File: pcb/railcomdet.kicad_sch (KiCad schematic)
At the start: 43 parts, among them J1 MVE252-5-V, J10 MVE252-5-V, J2 MVE252-5-V, J3 MVE252-5-V, J7 MVE252-5-V, J8 MVE252-5-V, J9 MVE252-5-V, U1 VO0631T, U2 VO0631T, U3 VO0631T

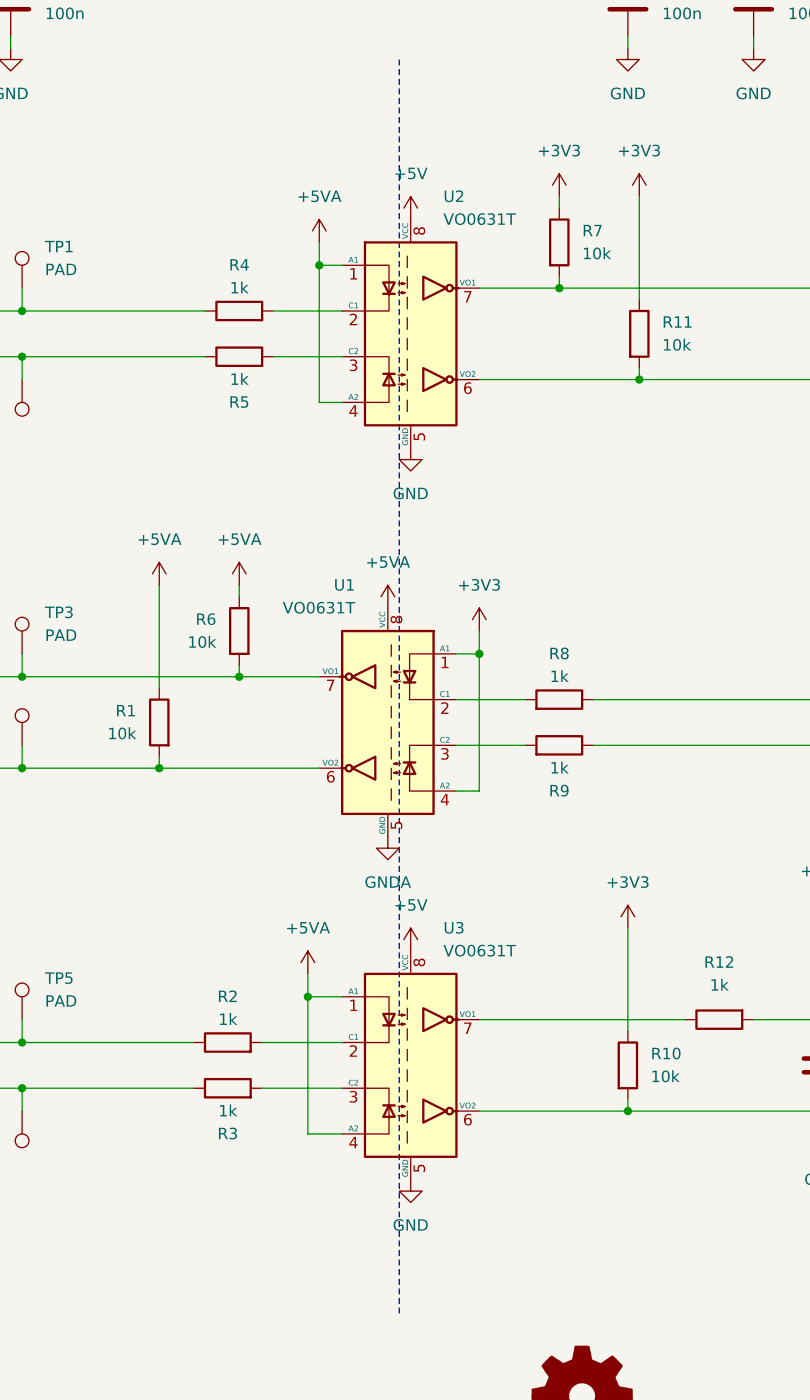
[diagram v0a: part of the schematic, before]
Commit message: Added Sch.diodes, text editing..
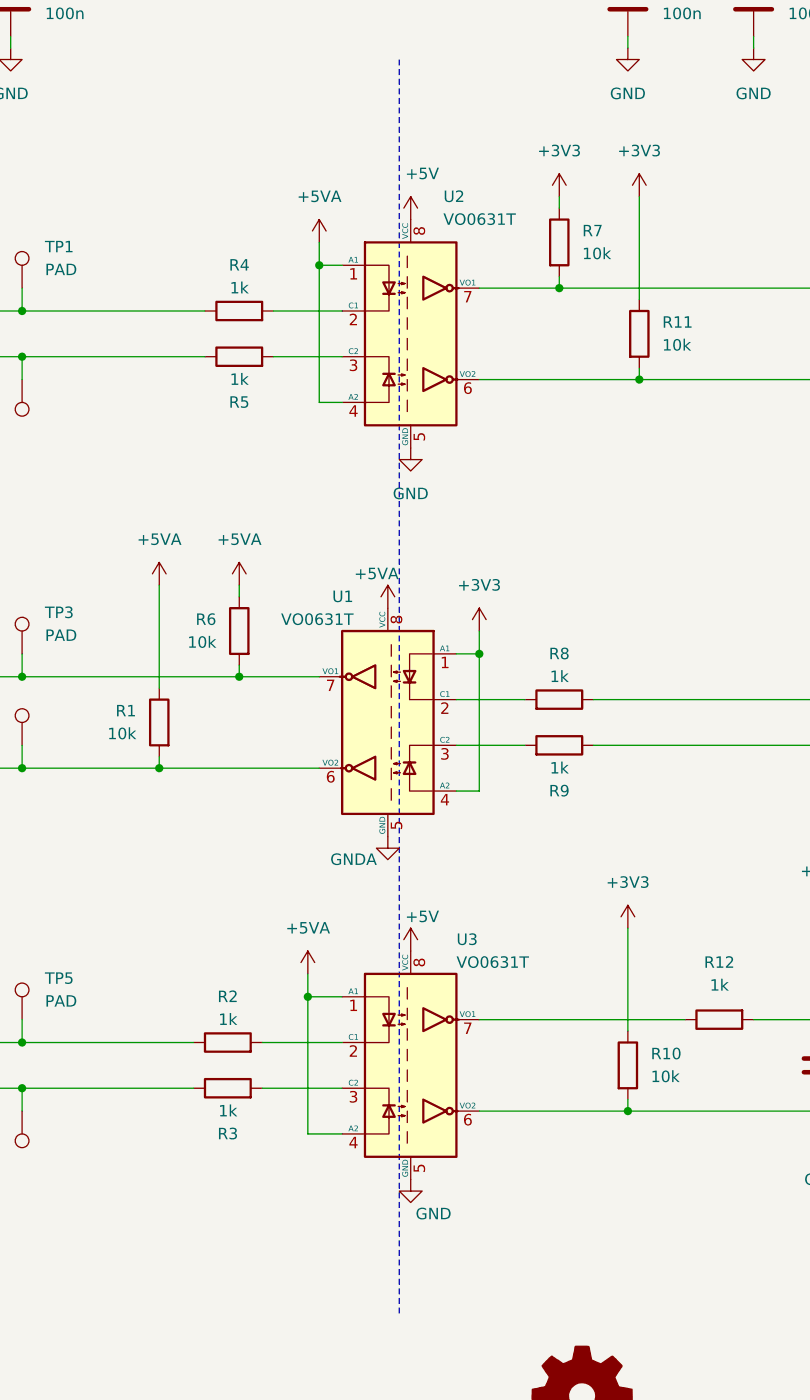
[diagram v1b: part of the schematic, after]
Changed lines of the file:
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@@
   )
   (symbol (lib_id "Isolator:VO0631T") (at 143.51 106.68 0) (mirror y) (unit 1)
-    (in_bom yes) (on_board yes) (dnp no) (fields_autoplaced)
-    (property "Reference" "U1" (at 139.8839 91.44 0)
-      (effects (font (size 1.27 1.27)) (justify left))
-    )
-    (property "Value" "VO0631T" (at 139.8839 93.98 0)
+    (in_bom yes) (on_board yes) (dnp no)
+    (property "Reference" "U1" (at 139.7 92.71 0)
+      (effects (font (size 1.27 1.27)) (justify left))
+    )
+    (property "Value" "VO0631T" (at 139.7 95.25 0)
       (effects (font (size 1.27 1.27)) (justify left))
     )
@@
   )
   (symbol (lib_id "power:GND") (at 146.05 157.48 0) (unit 1)
-    (in_bom yes) (on_board yes) (dnp no) (fields_autoplaced)
+    (in_bom yes) (on_board yes) (dnp no)
     (property "Reference" "#PWR012" (at 146.05 163.83 0)
       (effects (font (size 1.27 1.27)) hide)
     )
-    (property "Value" "GND" (at 146.05 162.56 0)
+    (property "Value" "GND" (at 148.59 161.29 0)
       (effects (font (size 1.27 1.27)))
     )
@@
   )
   (symbol (lib_id "Isolator:VO0631T") (at 146.05 144.78 0) (unit 1)
-    (in_bom yes) (on_board yes) (dnp no) (fields_autoplaced)
-    (property "Reference" "U3" (at 149.6761 129.54 0)
-      (effects (font (size 1.27 1.27)) (justify left))
-    )
-    (property "Value" "VO0631T" (at 149.6761 132.08 0)
+    (in_bom yes) (on_board yes) (dnp no)
+    (property "Reference" "U3" (at 151.13 130.81 0)
+      (effects (font (size 1.27 1.27)) (justify left))
+    )
+    (property "Value" "VO0631T" (at 151.13 133.35 0)
       (effects (font (size 1.27 1.27)) (justify left))
     )
@@
   )
   (symbol (lib_id "power:+5VA") (at 143.51 93.98 0) (unit 1)
-    (in_bom yes) (on_board yes) (dnp no) (fields_autoplaced)
+    (in_bom yes) (on_board yes) (dnp no)
     (property "Reference" "#PWR07" (at 143.51 97.79 0)
       (effects (font (size 1.27 1.27)) hide)
     )
-    (property "Value" "+5VA" (at 143.51 88.9 0)
+    (property "Value" "+5VA" (at 142.24 90.17 0)
       (effects (font (size 1.27 1.27)))
     )
@@
   )
   (symbol (lib_id "power:+5V") (at 146.05 50.8 0) (unit 1)
-    (in_bom yes) (on_board yes) (dnp no) (fields_autoplaced)
+    (in_bom yes) (on_board yes) (dnp no)
     (property "Reference" "#PWR09" (at 146.05 54.61 0)
       (effects (font (size 1.27 1.27)) hide)
     )
-    (property "Value" "+5V" (at 146.05 45.72 0)
+    (property "Value" "+5V" (at 147.32 45.72 0)
       (effects (font (size 1.27 1.27)))
     )
@@
       (effects (font (size 1.27 1.27)) hide)
     )
-    (property "Value" "GNDA" (at 143.51 124.46 0)
+    (property "Value" "GNDA" (at 139.7 121.92 0)
       (effects (font (size 1.27 1.27)))
     )
@@
   )
   (symbol (lib_id "power:+5V") (at 146.05 132.08 0) (unit 1)
-    (in_bom yes) (on_board yes) (dnp no) (fields_autoplaced)
+    (in_bom yes) (on_board yes) (dnp no)
     (property "Reference" "#PWR011" (at 146.05 135.89 0)
       (effects (font (size 1.27 1.27)) hide)
     )
-    (property "Value" "+5V" (at 146.05 127 0)
-      (effects (font (size 1.27 1.27)))
-    )
+    (property "Value" "+5V" (at 147.32 128.27 0)
+      (effects (font (size 1.27 1.27)))
+    )

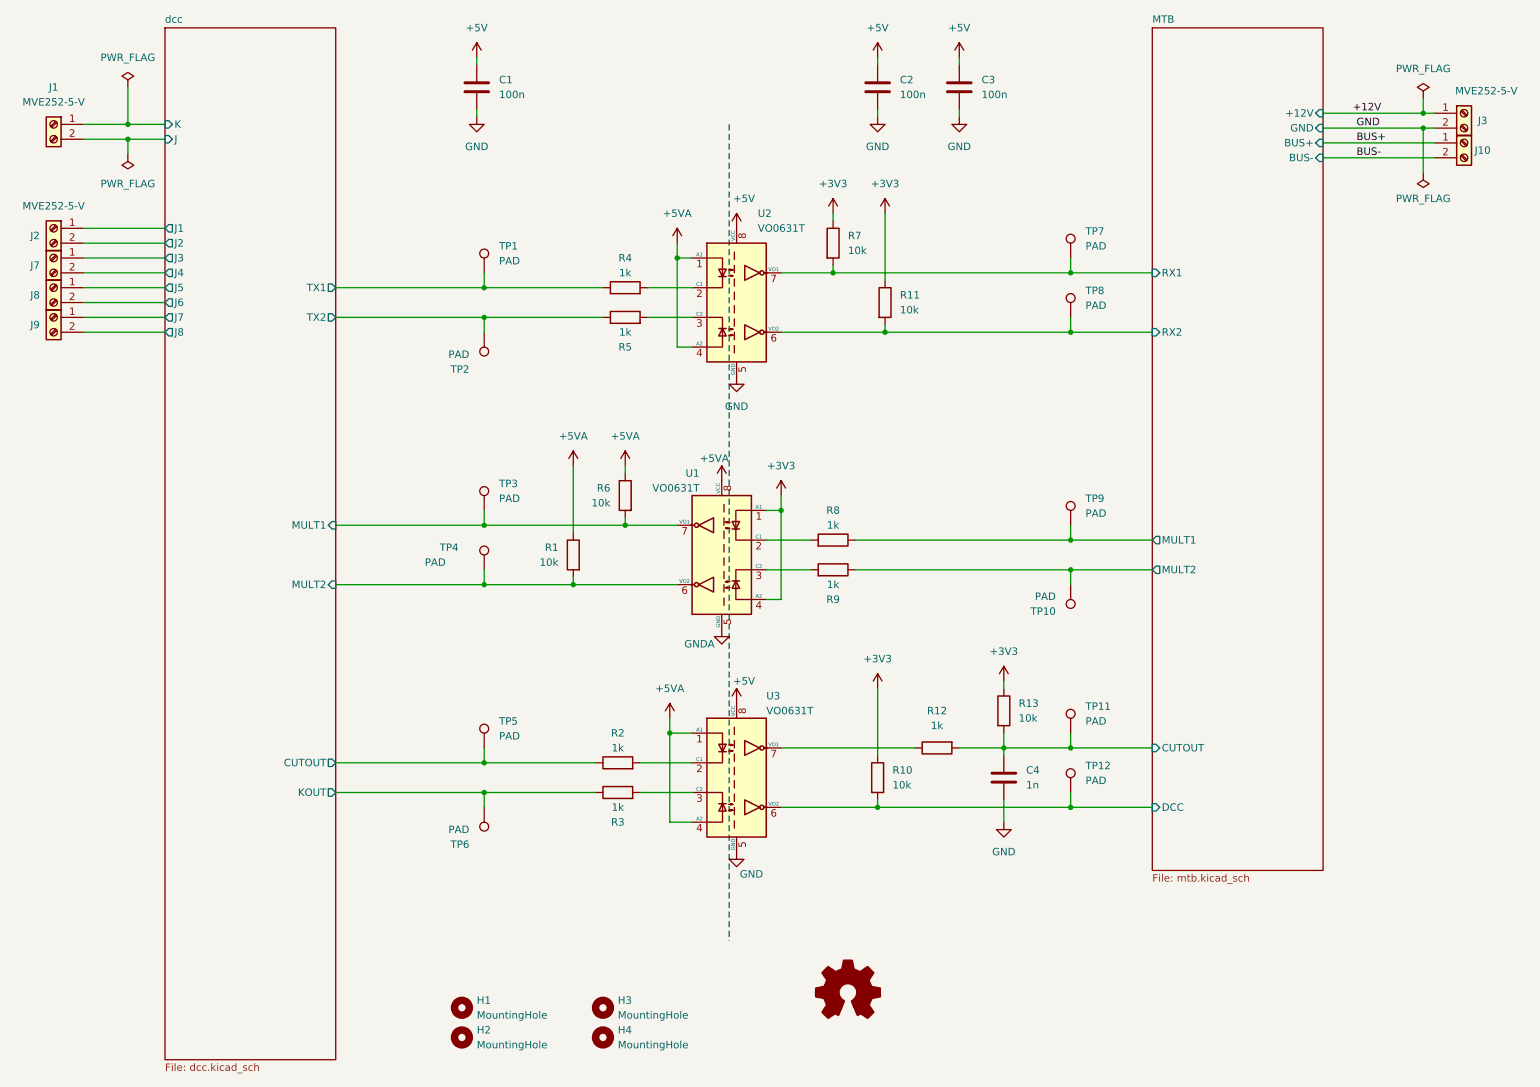
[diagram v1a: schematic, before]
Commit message: root: rotate test points same way.
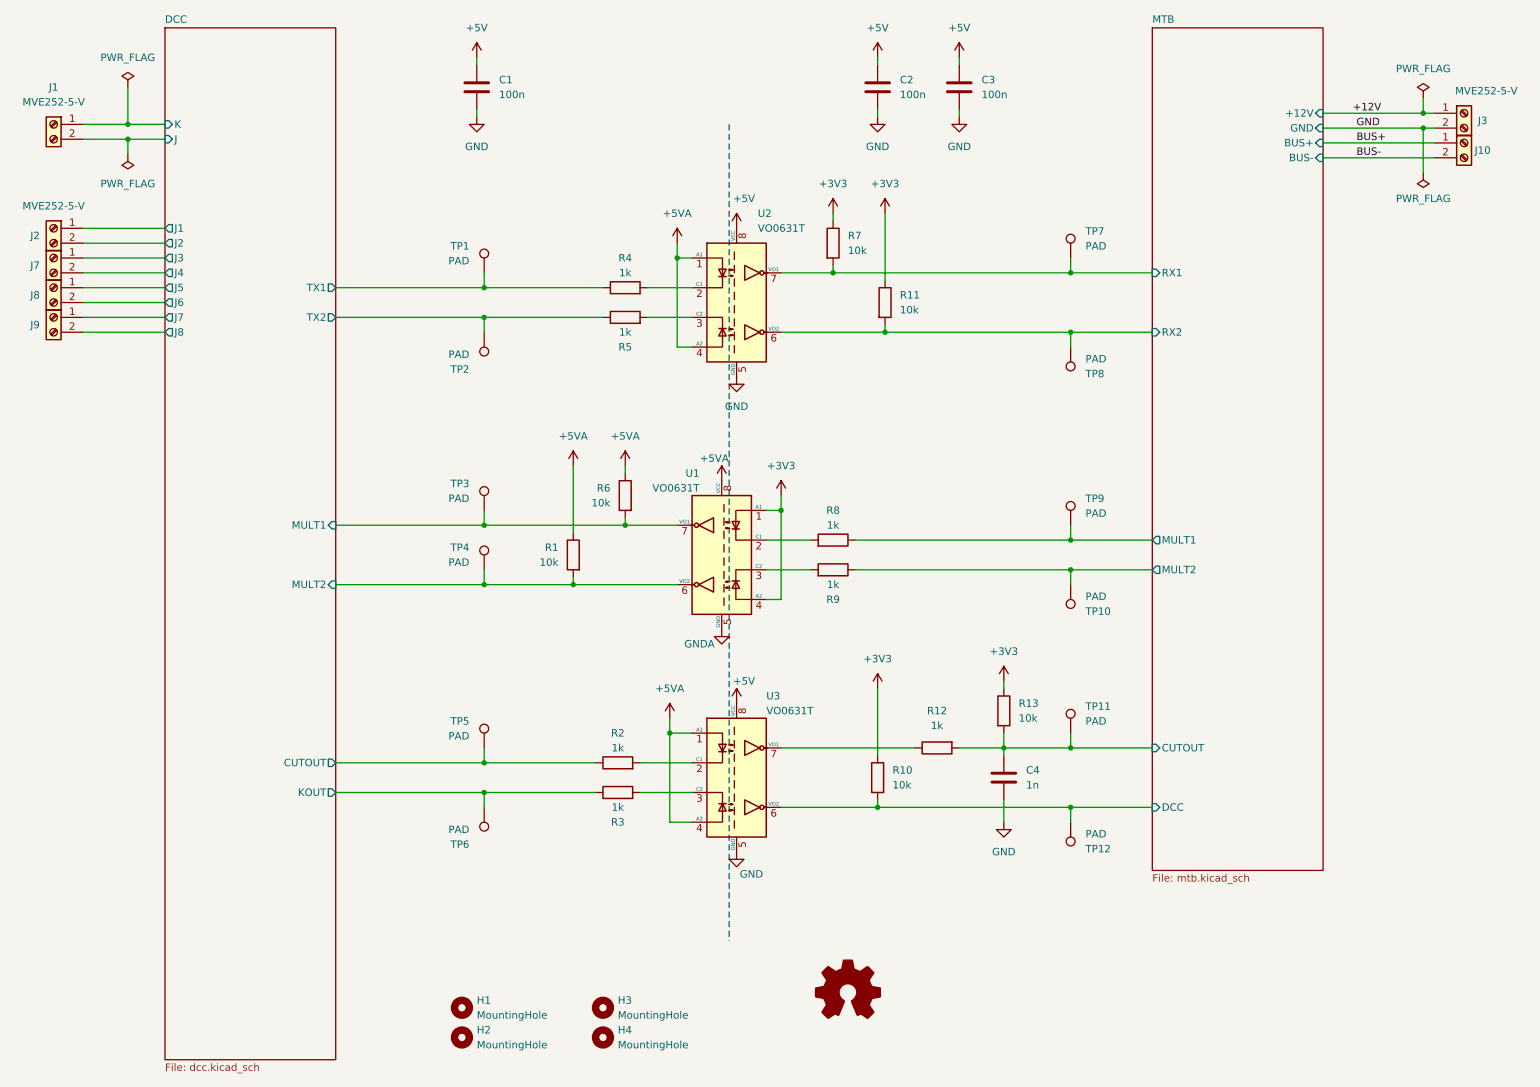
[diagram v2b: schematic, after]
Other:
- sheet dcc renamed DCC
- moved on the sheet: TP10, TP12, TP8
